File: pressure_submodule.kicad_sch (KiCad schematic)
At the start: 17 parts, among them J3 Conn_01x04, Q1 BSZ0902NSATMA1, U2 INA180

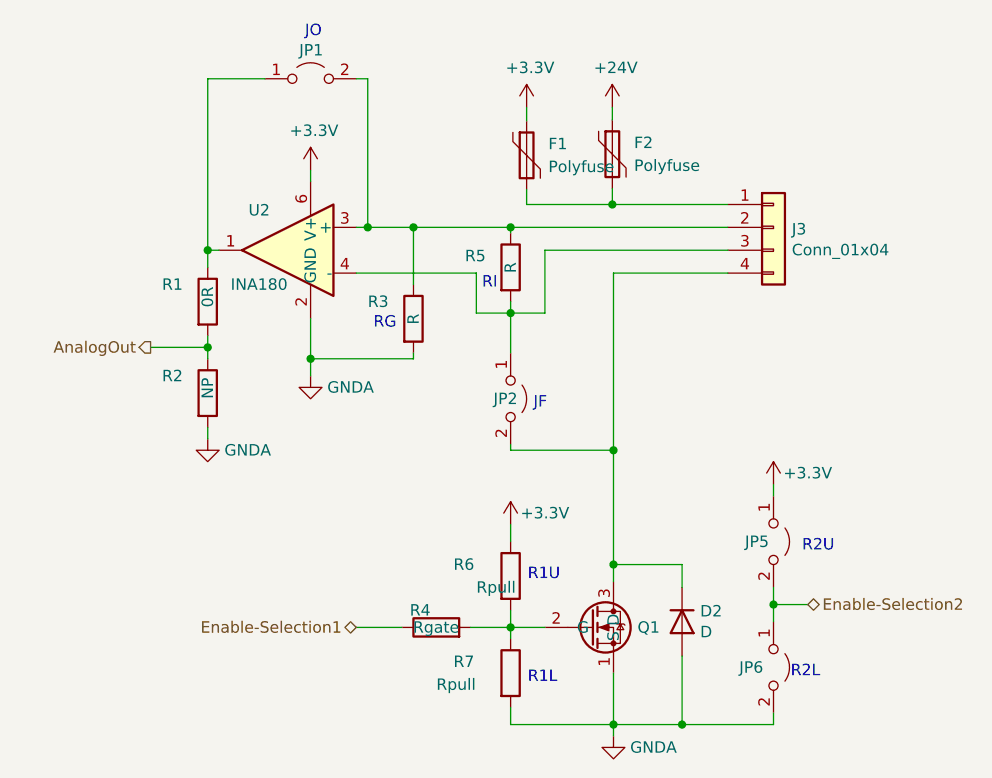
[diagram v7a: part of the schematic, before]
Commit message: Connectors routed
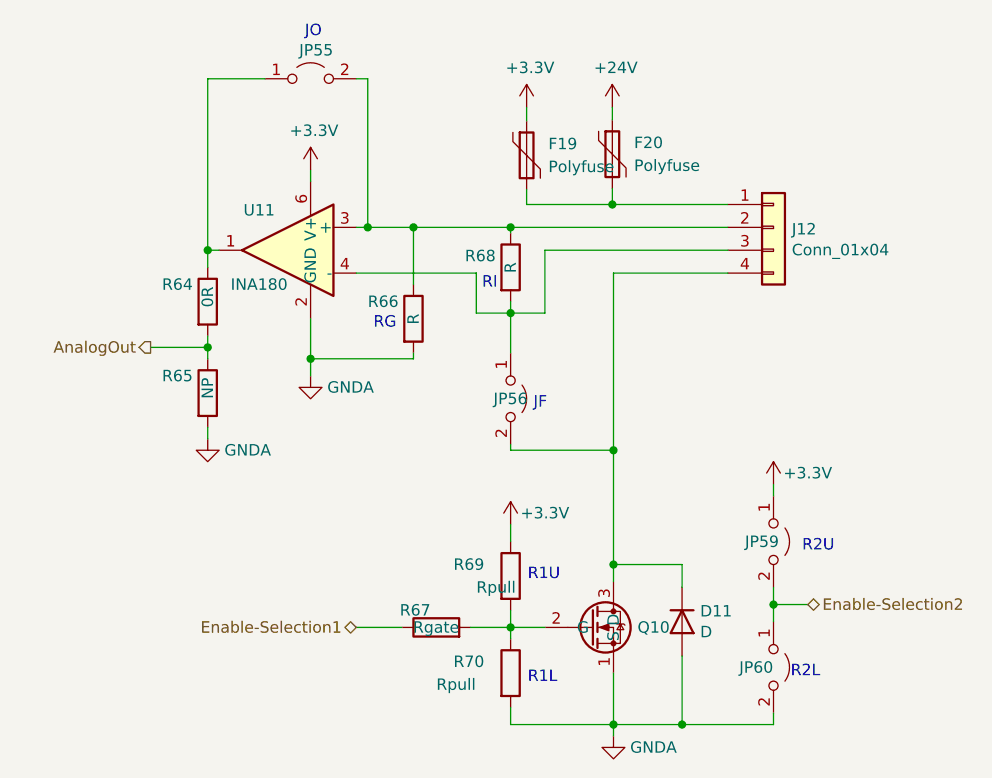
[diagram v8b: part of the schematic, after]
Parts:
- renumbered D2 to D11, F1 to F19, F2 to F20, J3 to J12, JP1 to JP55, JP2 to JP56, JP5 to JP59, JP6 to JP60, Q1 to Q10, R1 to R64, R2 to R65, R3 to R66, R4 to R67, R5 to R68, R6 to R69, R7 to R70, U2 to U11
